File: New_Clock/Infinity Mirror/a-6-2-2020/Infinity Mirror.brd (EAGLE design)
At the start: 81 x 26 mm, 20 parts, among them IC1 MSGEQ7P, J1 Vsupply, J3 LED, J4 LED_CAP, U1 DS1307, Y1 32.768kHz

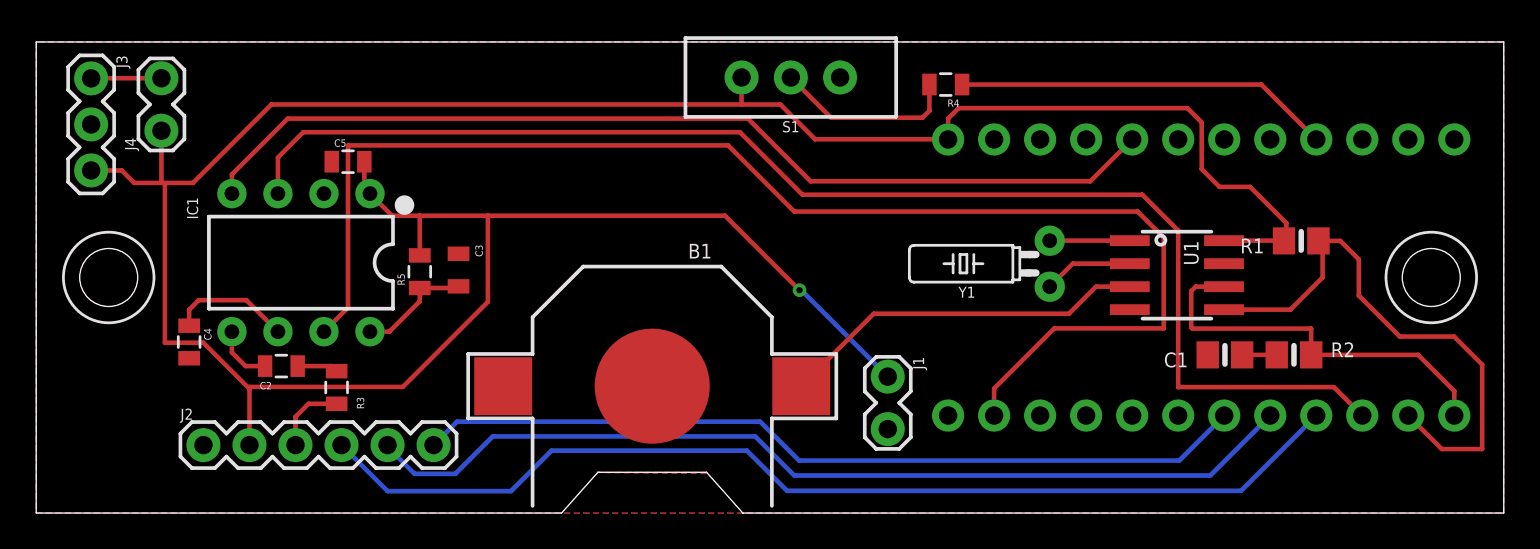
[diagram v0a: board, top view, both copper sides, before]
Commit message: added test code for board-a proving that the clock, 3 analog inputs, daylight-savings time switch and msgeq7 and leds work
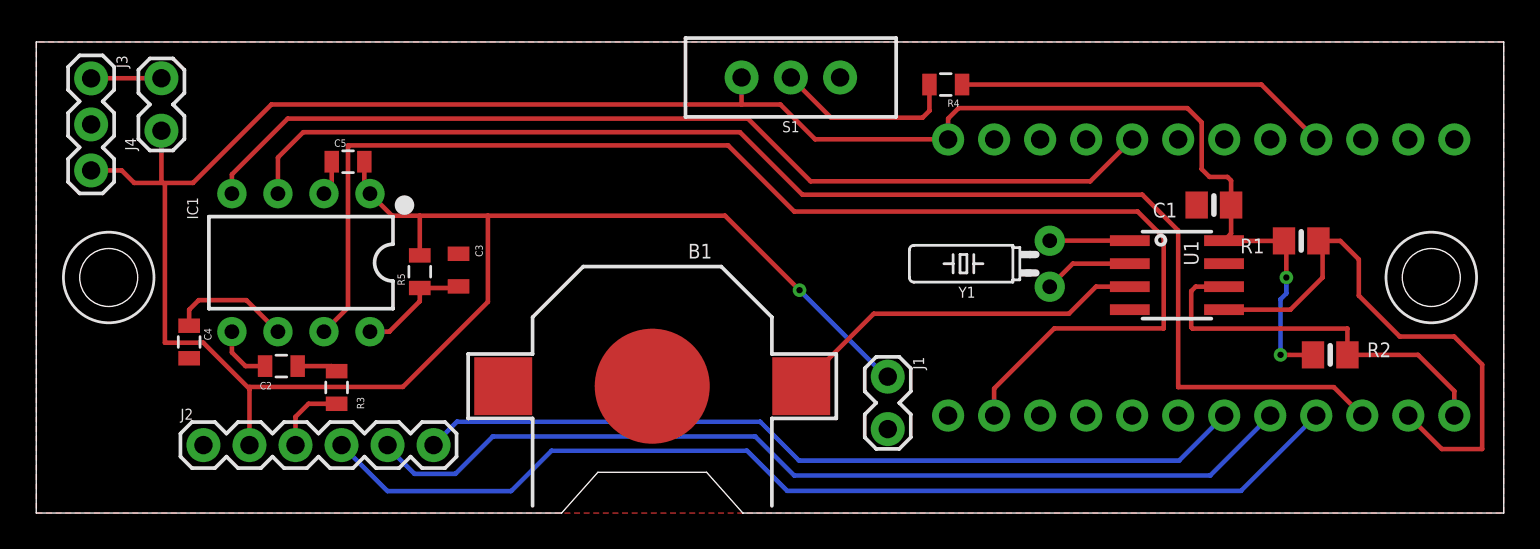
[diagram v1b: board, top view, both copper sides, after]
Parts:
- J2: value (none) -> AUDIO_POTS
- moved C1 8.29 mm to (65.0, 17.0)
- moved R2 2.00 mm to (71.4, 8.73)
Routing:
- net VCC: track 159.9 -> 164.3 mm, vias 1 -> 3
- net XO: track 6.95 -> 4.95 mm
- net GND: track 4.49 -> 5.82 mm
- removed copper zone on layer 16, net GND
